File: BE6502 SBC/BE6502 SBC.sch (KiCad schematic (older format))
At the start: 55 parts, among them J1 Expansion, J2 CLOCK_SEL, J3 BARREL_JACK, M1 Mounting, M2 Mounting, M3 Mounting, M4 Mounting, SW1 RESET, SW2 MIDDLE, SW3 UP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

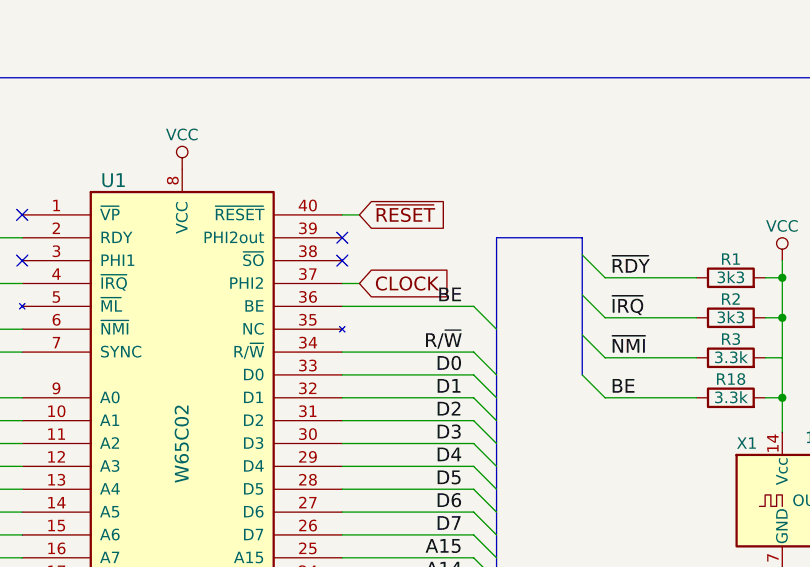
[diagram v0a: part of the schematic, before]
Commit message: Cosmetic schematic tweak
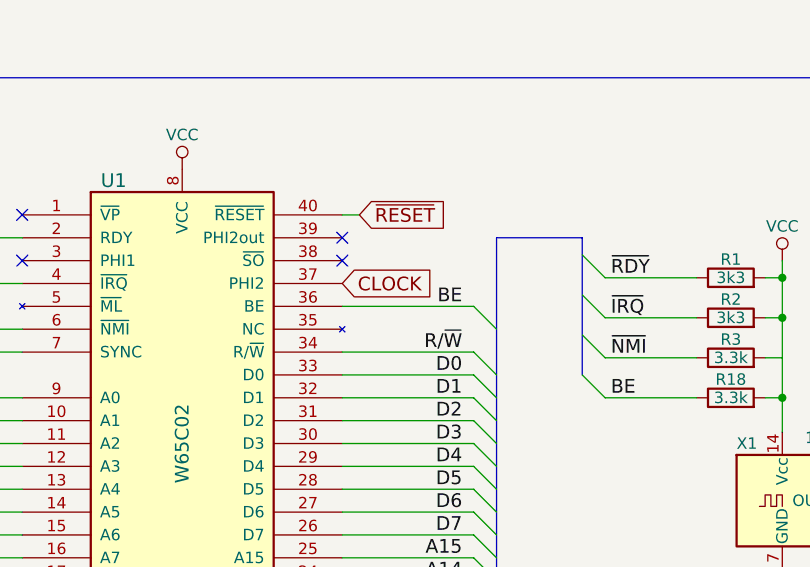
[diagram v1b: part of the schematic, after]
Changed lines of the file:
@@
 ~NMI
 NoConn ~ 3275 1650
-Text GLabel 3350 1850 2    60   Input ~ 0
+Text GLabel 3275 1850 2    60   Input ~ 0
 CLOCK
-Wire Wire Line
-	3350 1850 3275 1850
 Text GLabel 6000 2900 0    60   Output ~ 0
 CLOCK

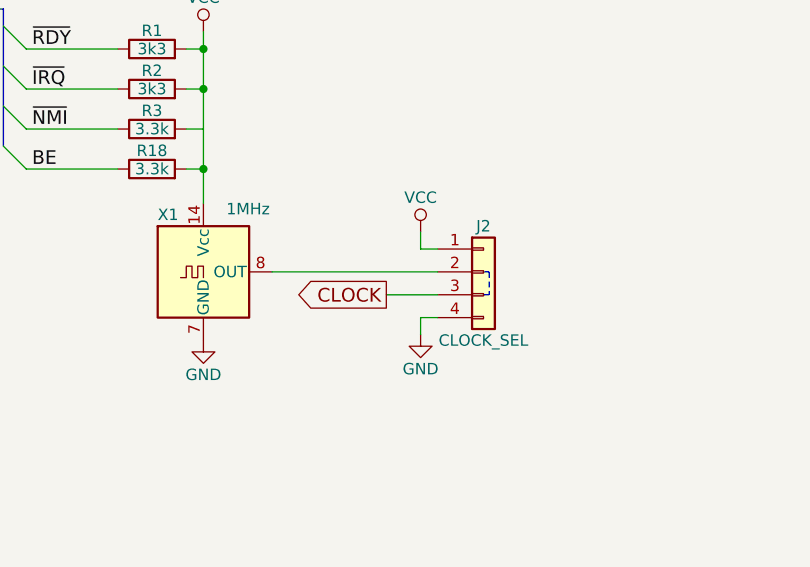
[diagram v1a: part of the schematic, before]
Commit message: Added current limiting resistor in case more than one clock accidentally activated at the same time
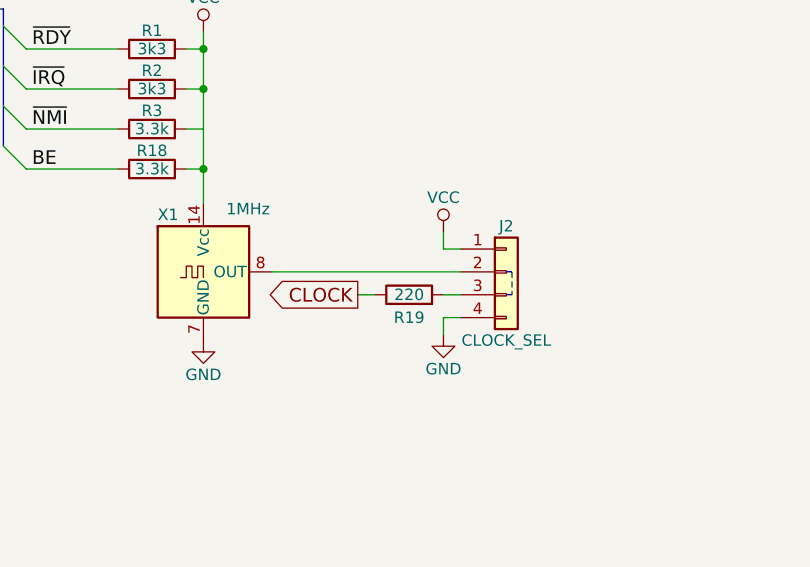
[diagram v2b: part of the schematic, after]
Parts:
- added R19: 220, Resistors_THT:R_Axial_DIN0207_L6.3mm_D2.5mm_P10.16mm_Horizontal, symbol Device:R
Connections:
- net CLOCK: now also R19.1; no longer J2.3 (Pin_3)
- new net: J2.3 (Pin_3), R19.2
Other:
- moved on the sheet: J2
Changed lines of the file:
@@
 Text GLabel 3275 1850 2    60   Input ~ 0
 CLOCK
-Text GLabel 6000 2900 0    60   Output ~ 0
+Text GLabel 5875 2900 0    60   Output ~ 0
 CLOCK
-Wire Wire Line
-	5500 2800 6225 2800
 $Comp
 L switches:SW_Push SW1
@@
 L conn:Conn_01x04 J2
 U 1 1 5DC631B0
-P 6425 2800
-F 0 "J2" H 6425 3000 50  0000 C CNN
-F 1 "CLOCK_SEL" H 6425 2500 50  0000 C CNN
-F 2 "Pin_Headers:Pin_Header_Angled_1x04_Pitch2.54mm" H 6425 2800 50  0001 C CNN
-F 3 "" H 6425 2800 50  0001 C CNN
-	1    6425 2800
+P 6525 2800
+F 0 "J2" H 6525 3000 50  0000 C CNN
+F 1 "CLOCK_SEL" H 6525 2500 50  0000 C CNN
+F 2 "Pin_Headers:Pin_Header_Angled_1x04_Pitch2.54mm" H 6525 2800 50  0001 C CNN
+F 3 "" H 6525 2800 50  0001 C CNN
+	1    6525 2800
 	1    0    0    -1
 $EndComp
@@
 L power:VCC #PWR028
 U 1 1 5DC63488
-P 6150 2625
-F 0 "#PWR028" H 6150 2475 50  0001 C CNN
-F 1 "VCC" H 6150 2775 50  0000 C CNN
-F 2 "" H 6150 2625 50  0001 C CNN
-F 3 "" H 6150 2625 50  0001 C CNN
-	1    6150 2625
-	1    0    0    -1
-$EndComp
-Wire Wire Line
-	6150 2625 6150 2700
-Wire Wire Line
-	6150 2700 6225 2700
-Wire Wire Line
-	6225 3000 6150 3000
-Wire Wire Line
-	6150 3000 6150 3075
+P 6250 2625
+F 0 "#PWR028" H 6250 2475 50  0001 C CNN
+F 1 "VCC" H 6250 2775 50  0000 C CNN
+F 2 "" H 6250 2625 50  0001 C CNN
+F 3 "" H 6250 2625 50  0001 C CNN
+	1    6250 2625
+	1    0    0    -1
+$EndComp
+Wire Wire Line
+	6250 2625 6250 2700
+Wire Wire Line
+	6250 2700 6325 2700
+Wire Wire Line
+	6325 3000 6250 3000
+Wire Wire Line
+	6250 3000 6250 3075
 $Comp
 L power:GND #PWR029
 U 1 1 5DC639FF
-P 6150 3075
-F 0 "#PWR029" H 6150 2825 50  0001 C CNN
-F 1 "GND" H 6150 2925 50  0000 C CNN
-F 2 "" H 6150 3075 50  0001 C CNN
-F 3 "" H 6150 3075 50  0001 C CNN
-	1    6150 3075
+P 6250 3075
+F 0 "#PWR029" H 6250 2825 50  0001 C CNN
+F 1 "GND" H 6250 2925 50  0000 C CNN
+F 2 "" H 6250 3075 50  0001 C CNN
+F 3 "" H 6250 3075 50  0001 C CNN
+	1    6250 3075
 	-1   0    0    -1
 $EndComp
-Wire Wire Line
-	6225 2900 6000 2900
 Wire Notes Line
-	6425 2800 6450 2800
+	6525 2800 6550 2800
 Wire Notes Line
-	6450 2800 6450 2900
+	6550 2800 6550 2900
 Wire Notes Line
-	6450 2900 6425 2900
+	6550 2900 6525 2900
 Wire Bus Line
 	4025 9225 4025 11100
@@
 Wire Bus Line
 	14300 6750 14300 8750
+$Comp
+L Device:R R19
+U 1 1 5E512E35
+P 6100 2900
+F 0 "R19" V 6000 2900 50  0000 C CNN
+F 1 "220" V 6100 2900 50  0000 C CNN
+F 2 "Resistors_THT:R_Axial_DIN0207_L6.3mm_D2.5mm_P10.16mm_Horizontal" V 6030 2900 50  0001 C CNN
+F 3 "" H 6100 2900 50  0001 C CNN
+	1    6100 2900
+	0    -1   -1   0
+$EndComp
+Wire Wire Line
+	6325 2900 6250 2900
+Wire Wire Line
+	5875 2900 5950 2900
+Wire Wire Line
+	5500 2800 6325 2800
 Wire Bus Line
 	6300 8450 6300 8650

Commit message: Revised SBC to add reset circuit
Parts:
- added C7: 100nF, Capacitors_THT:C_Disc_D4.7mm_W2.5mm_P5.00mm, symbol Device:C
- added J4: Control, Pin_Headers:Pin_Header_Angled_1x06_Pitch2.54mm, symbol be6502_control:BE6502_Control
- added R20: 47k, Resistors_THT:R_Axial_DIN0207_L6.3mm_D2.5mm_P10.16mm_Horizontal, symbol Device:R
- added R21: 1k, Resistors_THT:R_Axial_DIN0207_L6.3mm_D2.5mm_P10.16mm_Horizontal, symbol Device:R
- added U7: LM555, Housings_DIP:DIP-8_W7.62mm_Socket_LongPads, symbol linear:LM555
- C6: value 100nF -> 220nF
- U6: footprint Displays:WC1602A -> lcd1602a:WC1602A
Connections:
- net GND: now also C7.2, J4.6 (GND), R20.2, U7.1 (GND); no longer SW1.1
- net PA0: now also J4.1 (MIDDLE)
- net PA1: now also J4.2 (UP)
- net PA2: now also J4.3 (DOWN)
- net PA3: now also J4.4 (LEFT)
- net PA4: now also J4.5 (RIGHT)
- net VCC: now also SW1.1, C7.1, U7.4 (R), U7.8 (VCC)
- net ~RESET: now also U7.7 (DIS); no longer C6.1, SW1.2
- new net: C6.1, R21.1, U7.2 (TR), U7.6 (THR)
- new net: R20.1, R21.2, SW1.2
- no-connect marks 10 -> 12
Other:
- note added: "Reset circuit from KIM-1"
- moved on the sheet: C1, C2, C3, C4, C5, C6, J1, R4, SW1
